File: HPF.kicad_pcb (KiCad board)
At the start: 2 copper layers, 100 x 100 mm, 140 parts, among them J1 CONN_COAXIAL, J2 CONN_COAXIAL, P1 J6/J1 Ctrl brd, Q1 BSS84, U1 7805D-Pack, U2 PGA103+

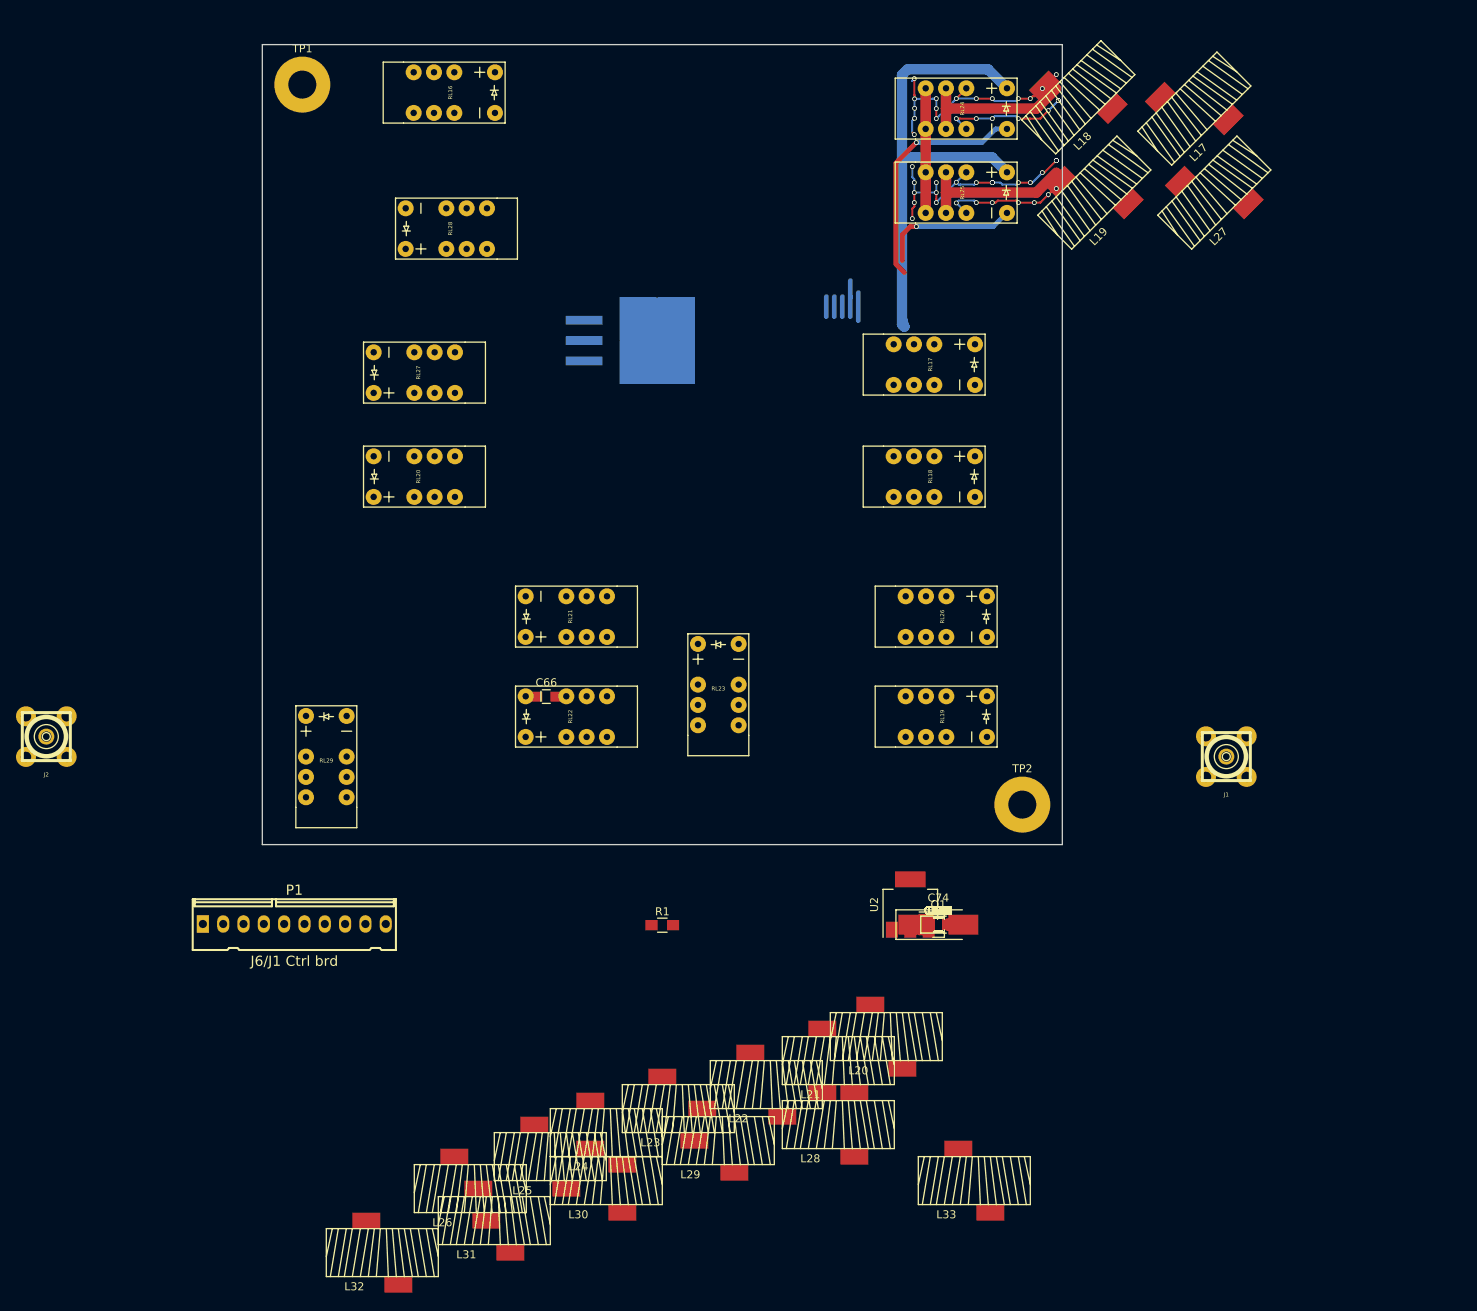
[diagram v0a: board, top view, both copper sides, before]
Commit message: firt routing, 6m LPF discarted
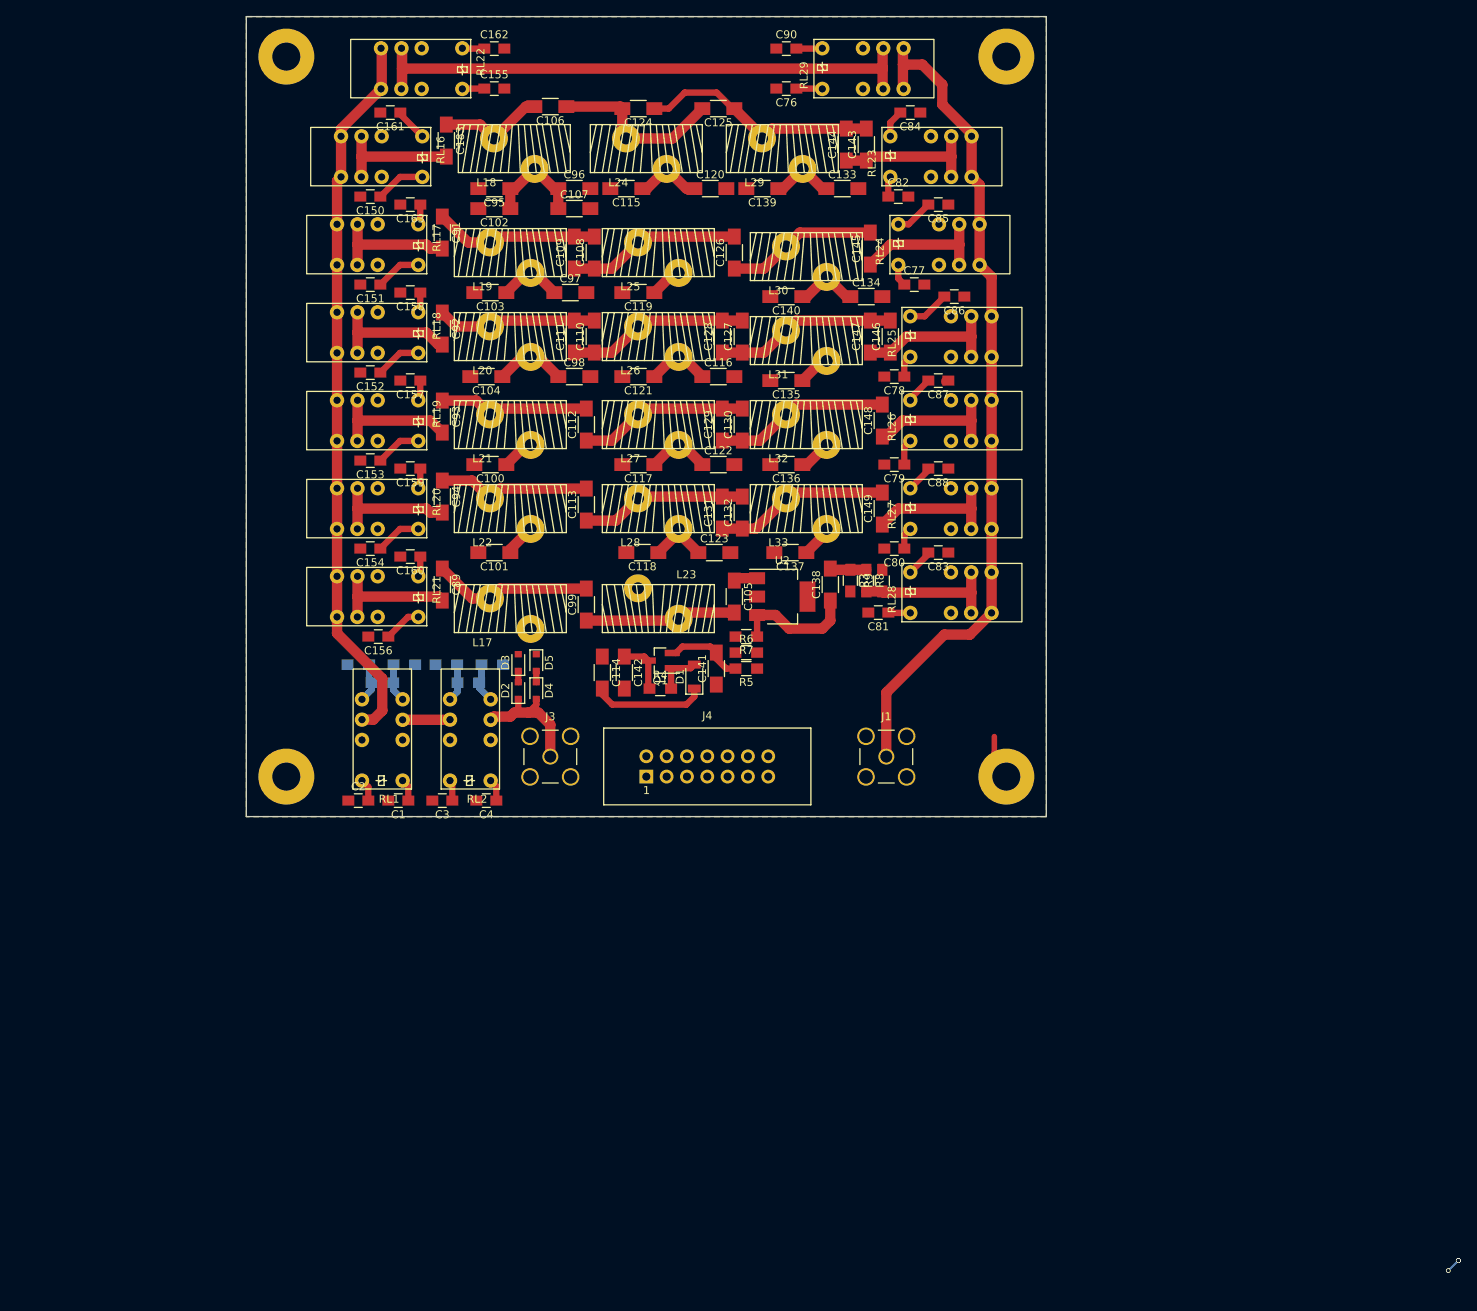
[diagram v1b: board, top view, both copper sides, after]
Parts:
- removed C66, C75: CP, Capacitors_SMD:C_0805_HandSoldering
- removed C74: CP, Capacitors_Tantalum_SMD:CP_Tantalum_Case-C_EIA-6032-28_Hand
- removed J2: CONN_COAXIAL, SMA_PINS:SMA_PINS
- removed P1: J6/J1 Ctrl brd, conn_kk100:kk100_22-23-2101
- removed U1: 7805D-Pack, TO_SOT_Packages_SMD:TO-263-3_TabPin4
- added C1: 10n, Capacitors_SMD:C_0805_HandSoldering, F.Cu at (109.0, 110.5)
- added C2: 10n, Capacitors_SMD:C_0805_HandSoldering, F.Cu at (104.0, 110.5)
- added C3: 10n, Capacitors_SMD:C_0805_HandSoldering, F.Cu at (114.5, 110.5)
- added C4: 10n, Capacitors_SMD:C_0805_HandSoldering, F.Cu at (120.0, 110.5)
- added D2: D, Diodes_SMD:D_0805, F.Cu at (124.0, 96.8)
- added D3: D, Diodes_SMD:D_0805, F.Cu at (124.0, 93.2)
- added D4: D, Diodes_SMD:D_0805, F.Cu at (126.2, 96.8)
- added D5: D, Diodes_SMD:D_0805, F.Cu at (126.2, 93.2)
- added J3: CONN_COAXIAL, Connectors:SMA_THT_Jack_Straight, F.Cu at (128.0, 105.0)
- added J4: CONN_01X13, Connectors:IDC_Header_Straight_14pins, F.Cu at (140.0, 107.5)
- added R10: R, Resistors_SMD:R_0805_HandSoldering, B.Cu at (107.0, 95.8)
- added R11: R, Resistors_SMD:R_0805_HandSoldering, B.Cu at (117.8, 95.8)
- added R12: R, Resistors_SMD:R_0805_HandSoldering, B.Cu at (115.0, 93.5)
- added R13: R, Resistors_SMD:R_0805_HandSoldering, B.Cu at (120.8, 93.5)
- added R2: R, Resistors_SMD:R_0805_HandSoldering, B.Cu at (109.8, 93.5)
- added RL1: EC2-12 NU, 2_Form_C_Relay:Relay_DPDT_NEC_EC2, F.Cu at (107.0, 108.0)
- added RL2: EC2-12 NU, 2_Form_C_Relay:Relay_DPDT_NEC_EC2, F.Cu at (118.0, 108.0)
- added TP3: TEST, Mounting_Holes:MountingHole_3.5mm_Pad, F.Cu at (95.0, 107.5)
- added TP4: TEST, Mounting_Holes:MountingHole_3.5mm_Pad, F.Cu at (185.0, 17.5)
- C100, C101, C102, C103, C104, C105, C106, C107, C108, C109, C110, C111, C112, C113, C114, C115, C116, C117, C118, C119, C120, C121, C122, C123, C124, C125, C126, C127, C128, C129, C130, C131, C132, C133, C134, C135, C136, C137, C138, C139, C140, C141, C142, C143, C144, C145, C146, C147, C148, C149, C183, C89, C91, C92, C93, C94, C95, C96, C97, C98, C99: footprint Capacitors_SMD:C_0805_HandSoldering -> Capacitors_SMD:C_1206_HandSoldering
- J1: footprint SMA_PINS:SMA_PINS -> Connectors:SMA_THT_Jack_Straight
- L17, L18, L19, L20, L21, L22, L23, L24, L25, L26, L27, L28, L29, L30, L31, L32, L33: footprint T50_V_cms:T50_V_smd -> T50:T50_V_THT
- R1: value 0 -> R; moved to B.Cu
- RL16, RL17, RL18, RL19, RL20, RL21, RL22, RL23, RL24, RL25, RL26, RL27, RL28, RL29: value EE2-5NU -> EC2-12 NU; footprint 2_Form_C_Relay:THT_2_formC -> 2_Form_C_Relay:Relay_DPDT_NEC_EC2
- moved L29 124.3 mm to (157.0, 29.0)
- moved L24 123.1 mm to (140.0, 29.0)
- moved C162 122.8 mm to (121.0, 16.5)
- moved C161 122.5 mm to (108.0, 24.5), turned to 180 degrees
- moved C155 118.3 mm to (121.0, 21.5)
- moved L30 118.2 mm to (160.0, 42.5)
- moved L31 116.7 mm to (160.0, 53.0)
- moved L32 116.3 mm to (160.0, 63.5)
- moved C183 115.7 mm to (115.0, 28.0), turned to 270 degrees
- moved C150 115.4 mm to (105.5, 35.0), turned to 180 degrees
- moved L25 113.8 mm to (141.5, 42.0)
- moved C106 113.2 mm to (128.0, 23.8), turned to 180 degrees
- moved C163 111.6 mm to (110.5, 36.0), turned to 180 degrees
- moved C90 111.1 mm to (157.5, 16.5)
- moved L26 109.1 mm to (141.5, 52.5)
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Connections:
- net 1.5 renamed 1.5HPF
- net 13 renamed 13HPF
- net 20 renamed 20HPF
- net 54 renamed 6mLNA
- net 6.5 renamed 6.5HPF
- net 9.5 renamed 9.5HPF
- net Bypass renamed HPF_ByPass
- C157 pad 1: +5V -> +12V
- C158 pad 1: +5V -> +12V
- C159 pad 1: +5V -> +12V
- C160 pad 1: +5V -> +12V
- C161 pad 1: +5V -> +12V
- C162 pad 1: +5V -> +12V
- C163 pad 1: +5V -> +12V
- C76 pad 1: +5V -> +12V
- C77 pad 1: +5V -> +12V
- C78 pad 1: +5V -> +12V
- C79 pad 1: +5V -> +12V
- C80 pad 1: +5V -> +12V
- C81 pad 1: +5V -> +12V
- C82 pad 1: +5V -> +12V
- R1 pad 1: (no net) -> Net-(R1-Pad1)
- R1 pad 2: Net-(P1-Pad7) -> GND
- RL16 pad 1: +5V -> +12V
- RL16 pad 5: Net-(J1-Pad1) -> Net-(RL1-Pad9)
- RL16 pad 8: Net-(J1-Pad1) -> Net-(RL1-Pad9)
- RL17 pad 1: +5V -> +12V
- RL17 pad 5: Net-(J1-Pad1) -> Net-(RL1-Pad9)
- RL17 pad 8: Net-(J1-Pad1) -> Net-(RL1-Pad9)
- RL18 pad 1: +5V -> +12V
- RL18 pad 5: Net-(J1-Pad1) -> Net-(RL1-Pad9)
- RL18 pad 8: Net-(J1-Pad1) -> Net-(RL1-Pad9)
- RL19 pad 1: +5V -> +12V
- RL19 pad 5: Net-(J1-Pad1) -> Net-(RL1-Pad9)
- RL19 pad 8: Net-(J1-Pad1) -> Net-(RL1-Pad9)
- RL20 pad 1: +5V -> +12V
- RL20 pad 5: Net-(J1-Pad1) -> Net-(RL1-Pad9)
- RL20 pad 8: Net-(J1-Pad1) -> Net-(RL1-Pad9)
- RL21 pad 1: +5V -> +12V
- RL21 pad 5: Net-(J1-Pad1) -> Net-(RL1-Pad9)
- RL21 pad 8: Net-(J1-Pad1) -> Net-(RL1-Pad9)
- RL22 pad 1: +5V -> +12V
- RL22 pad 5: Net-(J1-Pad1) -> Net-(RL1-Pad9)
- RL22 pad 8: Net-(J1-Pad1) -> Net-(RL1-Pad9)
- RL23 pad 1: +5V -> +12V
- RL23 pad 5: Net-(J2-Pad1) -> Net-(J1-Pad1)
- RL23 pad 8: Net-(J2-Pad1) -> Net-(J1-Pad1)
- RL24 pad 1: +5V -> +12V
- RL24 pad 5: Net-(J2-Pad1) -> Net-(J1-Pad1)
- RL24 pad 8: Net-(J2-Pad1) -> Net-(J1-Pad1)
- RL25 pad 1: +5V -> +12V
- RL25 pad 5: Net-(J2-Pad1) -> Net-(J1-Pad1)
- RL25 pad 8: Net-(J2-Pad1) -> Net-(J1-Pad1)
- RL26 pad 1: +5V -> +12V
- RL26 pad 5: Net-(J2-Pad1) -> Net-(J1-Pad1)
- RL26 pad 8: Net-(J2-Pad1) -> Net-(J1-Pad1)
- RL27 pad 1: +5V -> +12V
- RL27 pad 5: Net-(J2-Pad1) -> Net-(J1-Pad1)
- RL27 pad 8: Net-(J2-Pad1) -> Net-(J1-Pad1)
- RL28 pad 1: +5V -> +12V
- RL28 pad 5: Net-(J2-Pad1) -> Net-(J1-Pad1)
- RL28 pad 8: Net-(J2-Pad1) -> Net-(J1-Pad1)
- RL29 pad 1: +5V -> +12V
- RL29 pad 5: Net-(J2-Pad1) -> Net-(J1-Pad1)
- RL29 pad 8: Net-(J2-Pad1) -> Net-(J1-Pad1)
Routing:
- net Net-(J1-Pad1): track 0.00 -> 104.9 mm
- net Net-(RL1-Pad9): track 0.00 -> 91.0 mm
- net Net-(RL22-Pad4): track 0.00 -> 70.2 mm
- net GND: track 73.0 -> 2.92 mm, vias 34 -> 0
- net +5V: track 61.6 -> 6.77 mm
- net +12V: track 0.00 -> 45.5 mm
- net Net-(C124-Pad1): track 0.00 -> 30.4 mm
- net Net-(C127-Pad1): track 0.00 -> 22.7 mm
- net Net-(C110-Pad1): track 0.00 -> 22.7 mm
- net 6mLNA: track 0.00 -> 22.3 mm
- net Net-(C106-Pad1): track 0.00 -> 22.1 mm
- net Net-(C131-Pad1): track 0.00 -> 21.9 mm
- net Net-(C129-Pad1): track 0.00 -> 21.9 mm
- net Net-(C108-Pad1): track 0.00 -> 21.7 mm
- net Net-(C112-Pad1): track 0.00 -> 21.2 mm
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- added copper zone on B.Cu, net GND
- added copper zone on F.Cu, net GND
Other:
- copper layers 2 -> 4
- board text added: "Pure Signal"
- board text added: "RX1_Line"
